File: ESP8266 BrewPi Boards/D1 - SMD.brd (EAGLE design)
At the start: 43.6 x 43.8 mm, 20 parts, among them J1 RJ45-8X, Q1 BSS123, Q2 BSS123

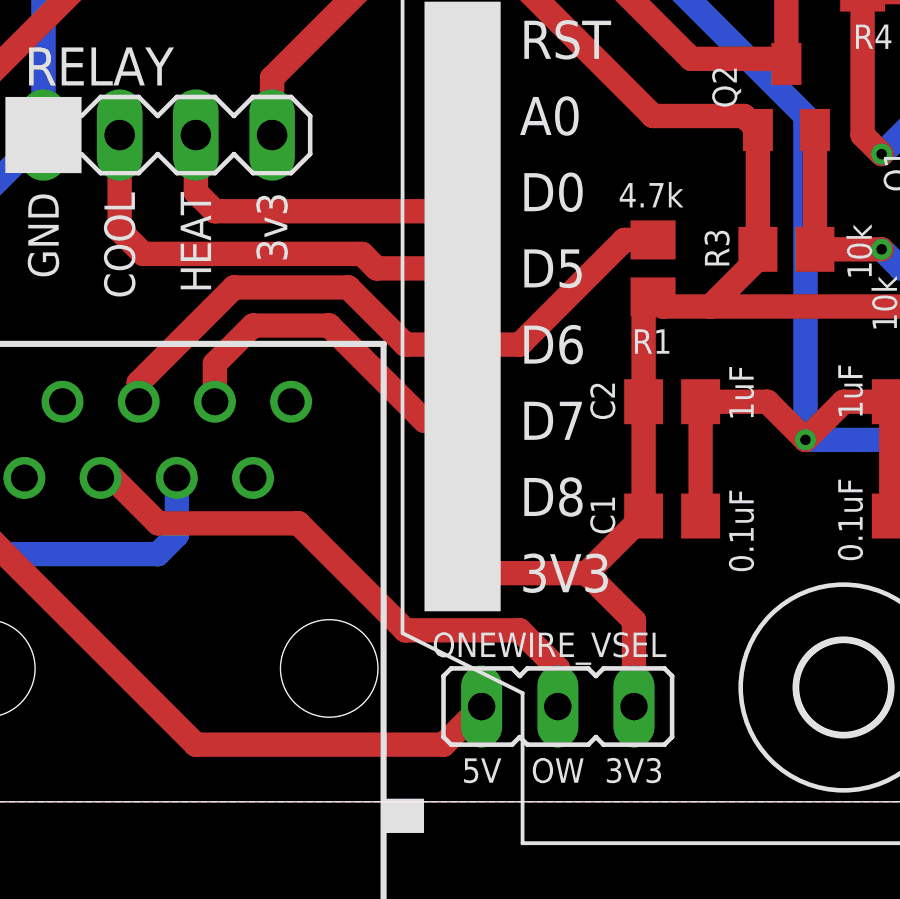
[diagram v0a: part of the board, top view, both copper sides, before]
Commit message: Add solder bridge to SMD board design
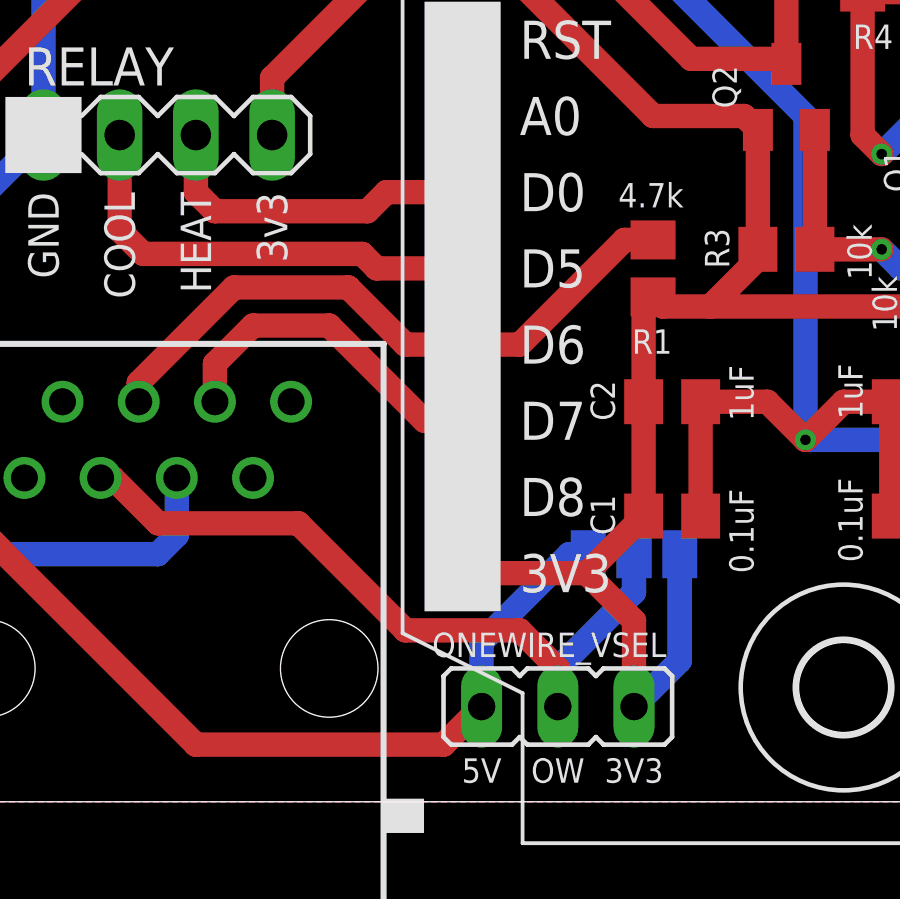
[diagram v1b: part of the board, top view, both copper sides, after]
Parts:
- added OW_VSEL: (no value), jumper:SJ_2
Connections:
- net 3V3: now also OW_VSEL.3
- net 5V: now also OW_VSEL.1
- net OW_VCC: now also OW_VSEL.2
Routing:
- net 5V: track 163.3 -> 170.2 mm
- net OW_VCC: track 19.1 -> 25.3 mm
- net 3V3: track 60.6 -> 66.3 mm
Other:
- board text added: "BrewPi D1 Mini SMD Breakout Board v1.2 @thorrak says hi"
- board text removed: "BrewPi D1 Mini SMD Breakout Board v1.1 @thorrak says hi"
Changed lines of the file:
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@@
 <grid distance="0.025" unitdist="inch" unit="inch" style="lines" multiple="1" display="no" altdistance="0.025" altunitdist="inch" altunit="inch"/>
 <layers>
-<layer number="1" name="Top" color="4" fill="1" visible="yes" active="yes"/>
+<layer number="1" name="Top" color="4" fill="1" visible="no" active="yes"/>
 <layer number="16" name="Bottom" color="1" fill="1" visible="yes" active="yes"/>
 <layer number="17" name="Pads" color="2" fill="1" visible="yes" active="yes"/>
@@
 <layer number="19" name="Unrouted" color="6" fill="1" visible="yes" active="yes"/>
 <layer number="20" name="Dimension" color="15" fill="1" visible="yes" active="yes"/>
-<layer number="21" name="tPlace" color="7" fill="1" visible="yes" active="yes"/>
+<layer number="21" name="tPlace" color="7" fill="1" visible="no" active="yes"/>
 <layer number="22" name="bPlace" color="7" fill="1" visible="yes" active="yes"/>
 <layer number="23" name="tOrigins" color="15" fill="1" visible="yes" active="yes"/>
 <layer number="24" name="bOrigins" color="15" fill="1" visible="yes" active="yes"/>
-<layer number="25" name="tNames" color="7" fill="1" visible="yes" active="yes"/>
-<layer number="26" name="bNames" color="7" fill="1" visible="yes" active="yes"/>
+<layer number="25" name="tNames" color="7" fill="1" visible="no" active="yes"/>
+<layer number="26" name="bNames" color="7" fill="1" visible="no" active="yes"/>
 <layer number="27" name="tValues" color="7" fill="1" visible="yes" active="yes"/>
 <layer number="28" name="bValues" color="7" fill="1" visible="yes" active="yes"/>
@@
 <text x="70.993" y="67.31" size="0.8128" layer="21" font="vector" ratio="12" rot="R270" align="top-right">GND In</text>
 <text x="81.28" y="62.23" size="1.016" layer="26" font="vector" ratio="12" rot="MR0">BrewPi D1 Mini SMD
-Breakout Board v1.1
+Breakout Board v1.2
 @thorrak says hi</text>
 <text x="44.45" y="60.325" size="1.016" layer="21" font="vector" ratio="12" rot="R90" align="center-right">GND</text>
@@
 <text x="49.53" y="60.325" size="1.016" layer="21" font="vector" ratio="12" rot="R90" align="center-right">SDA</text>
 <text x="52.07" y="60.325" size="1.016" layer="21" font="vector" ratio="12" rot="R90" align="center-right">SCL</text>
-<text x="79.375" y="38.735" size="1.016" layer="26" font="vector" ratio="12" rot="MR0">D0 - Heat
+<text x="79.375" y="50.165" size="1.016" layer="26" font="vector" ratio="12" rot="MR0">D0 - Heat
 D1 - I2C SCL
 D2 - I2C SDA
@@
 <text x="64.135" y="31.115" size="0.8128" layer="25" font="vector" ratio="12" align="bottom-center">3V3</text>
 <text x="61.595" y="31.115" size="0.8128" layer="25" font="vector" ratio="12" align="bottom-center">OW</text>
+<text x="64.135" y="40.005" size="0.8128" layer="26" font="vector" ratio="12" rot="MR0" align="bottom-center">OW</text>
+<text x="66.675" y="38.735" size="0.8128" layer="26" font="vector" ratio="12" rot="MR90" align="bottom-center">3V3</text>
+<text x="61.595" y="38.735" size="0.8128" layer="26" font="vector" ratio="12" rot="MR270" align="bottom-center">5V</text>
 </plain>
 <attributes>
@@
 <attribute name="VALUE" x="58.039" y="29.337" size="1.27" layer="27" ratio="10"/>
 </element>
+<element name="OW_VSEL" library="jumper" library_urn="urn:adsk.eagle:library:252" package="SJ_2" package3d_urn="urn:adsk.eagle:package:15474/1" value="" x="64.135" y="38.735" smashed="yes" rot="MR180">
+<attribute name="NAME" x="61.722" y="37.465" size="0.8128" layer="26" font="vector" ratio="10" rot="MR180"/>
+<attribute name="POPULARITY" value="7" x="64.135" y="38.735" size="1.778" layer="28" rot="MR180" display="off"/>
+<attribute name="VALUE" x="64.0349" y="38.735" size="0.02" layer="28" rot="MR180"/>
+</element>
 </elements>
 <signals>
@@
 <wire x1="46.99" y1="64.135" x2="53.34" y2="70.485" width="0.8128" layer="1"/>
 <wire x1="78.7" y1="71.755" x2="78.7" y2="67.27" width="0.8128" layer="1"/>
+<contactref element="OW_VSEL" pad="1"/>
+<wire x1="59.055" y1="33.655" x2="59.055" y2="35.814" width="0.8128" layer="16"/>
+<wire x1="61.976" y1="38.735" x2="59.055" y2="35.814" width="0.8128" layer="16"/>
+<wire x1="61.976" y1="38.735" x2="62.611" y2="38.735" width="0.8128" layer="16"/>
 </signal>
 <signal name="D6">
@@
 <contactref element="SV1" pad="3"/>
 <contactref element="U$1" pad="D0"/>
-<wire x1="58.42" y1="50.8" x2="57.785" y2="50.165" width="0.8128" layer="1"/>
+<wire x1="58.42" y1="50.8" x2="55.88" y2="50.8" width="0.8128" layer="1"/>
+<wire x1="55.88" y1="50.8" x2="55.245" y2="50.165" width="0.8128" layer="1"/>
 <wire x1="50.165" y1="50.165" x2="49.53" y2="50.8" width="0.8128" layer="1"/>
 <wire x1="49.53" y1="50.8" x2="49.53" y2="52.705" width="0.8128" layer="1"/>
-<wire x1="57.785" y1="50.165" x2="50.165" y2="50.165" width="0.8128" layer="1"/>
+<wire x1="55.245" y1="50.165" x2="50.165" y2="50.165" width="0.8128" layer="1"/>
 </signal>
 <signal name="3V3_SCL">
@@
 <wire x1="64.135" y1="33.655" x2="64.135" y2="36.515" width="0.8128" layer="1"/>
 <wire x1="64.135" y1="36.515" x2="62.55" y2="38.1" width="0.8128" layer="1"/>
+<contactref element="OW_VSEL" pad="3"/>
+<wire x1="64.135" y1="33.655" x2="65.659" y2="35.179" width="0.8128" layer="16"/>
+<wire x1="65.659" y1="38.735" x2="65.659" y2="35.179" width="0.8128" layer="16"/>
 </signal>
 <signal name="OW_VCC">
@@
 <wire x1="60.325" y1="36.195" x2="61.595" y2="34.925" width="0.8128" layer="1"/>
 <wire x1="61.595" y1="33.655" x2="61.595" y2="34.925" width="0.8128" layer="1"/>
+<contactref element="OW_VSEL" pad="2"/>
+<wire x1="61.595" y1="33.655" x2="61.595" y2="34.925" width="0.8128" layer="16"/>
+<wire x1="61.595" y1="34.925" x2="64.135" y2="37.465" width="0.8128" layer="16"/>
+<wire x1="64.135" y1="37.465" x2="64.135" y2="38.735" width="0.8128" layer="16"/>
 </signal>
 </signals>
@@
 <mfgpreviewcolor name="substratecolor" color="0xFF786E46"/>
 </mfgpreviewcolors>
+<errors>
+</errors>
 </board>
 </drawing>
